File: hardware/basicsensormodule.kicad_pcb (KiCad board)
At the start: 2 copper layers, 130.2 x 52.1 mm, 76 parts, among them J102 SENSOR, J401 USART, J601 RJ45, J602 RJ45, U201 MCP2551-I/SN, U202 MCP2515-E/ST-SOIC18, U301 LM324, U401 ATMEGA328P-PU, U501 LM7805, Y201 16MHz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

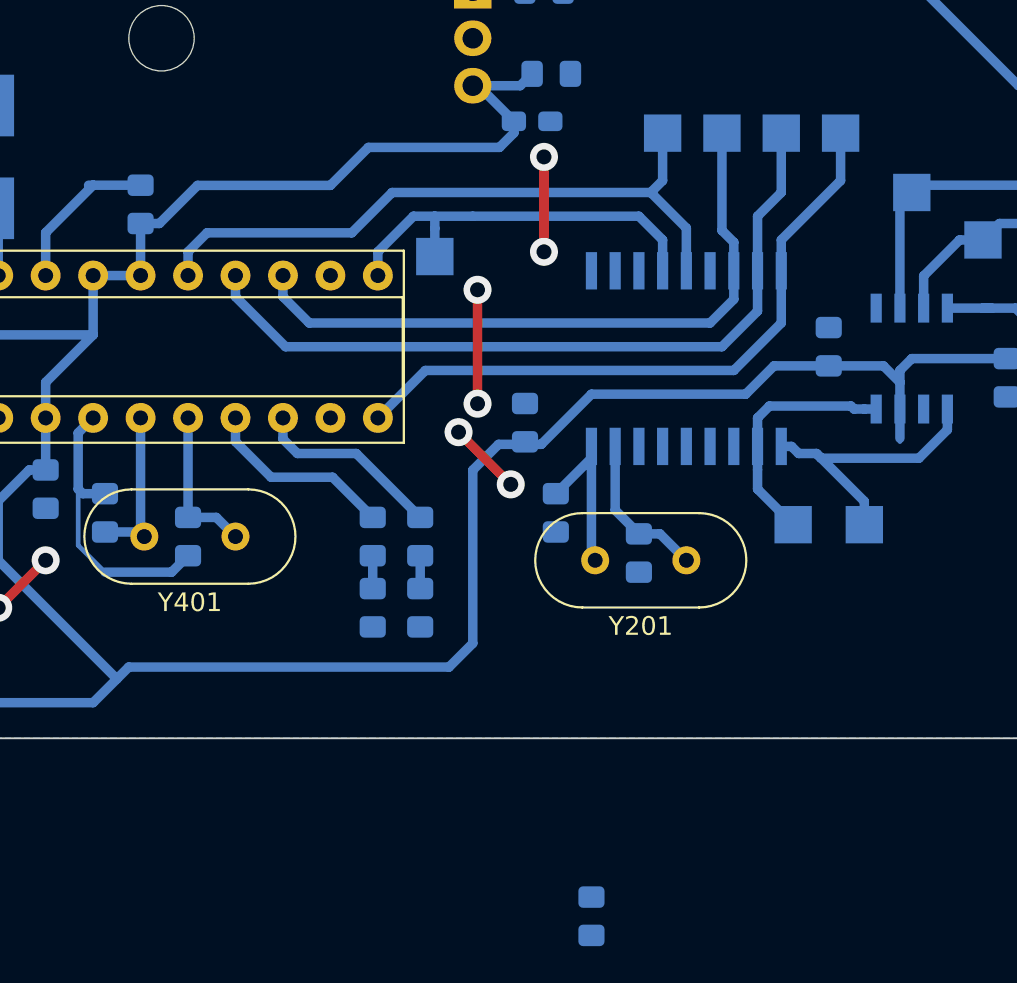
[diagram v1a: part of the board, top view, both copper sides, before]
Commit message: MCP2515 updated
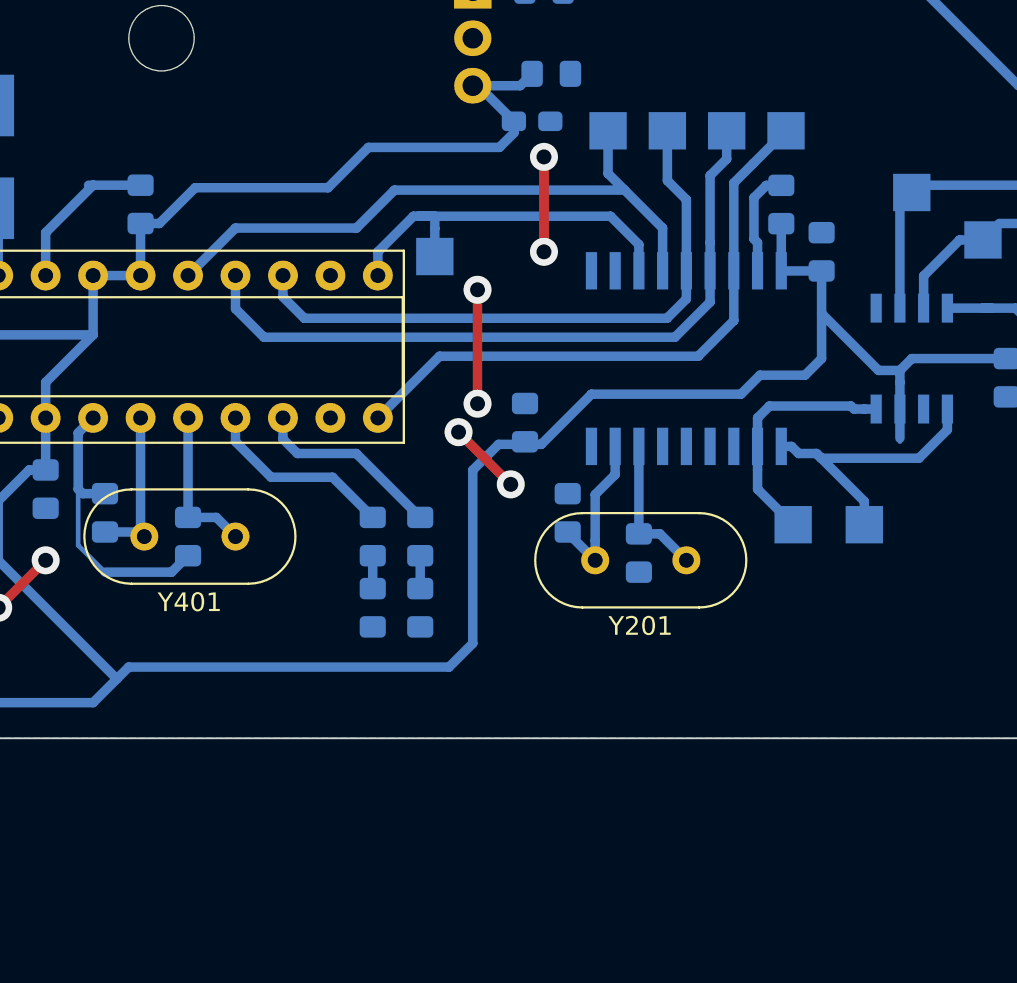
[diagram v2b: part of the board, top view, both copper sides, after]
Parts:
- U202: value MCP2515-E/ST-SOIC18 -> MCP2515-xSO
- moved R203 39.4 mm to (164.8, 96.3)
- moved C202 5.09 mm to (167.0, 98.8)
- moved TP206 2.92 mm to (155.6, 92.3)
- moved TP201 2.92 mm to (158.8, 92.3)
- moved TP202 2.92 mm to (161.9, 92.3)
- moved TP205 2.92 mm to (165.1, 92.3)
- moved C204 0.63 mm to (153.4, 112.8), turned to 90 degrees
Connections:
- U202 pad 10: GND -> Net-(U202-Pad10)
- U202 pad 12: Net-(U202-Pad12) -> /CANBUS/INT
- U202 pad 13: /CANBUS/INT -> /SCK
- U202 pad 14: /SCK -> /MOSI
- U202 pad 15: Net-(U202-Pad15) -> /MISO
- U202 pad 16: /MOSI -> /CANBUS/CS
- U202 pad 17: /MISO -> Net-(R203-Pad2)
- U202 pad 18: /CANBUS/CS -> +5V
- U202 pad 7: Net-(U202-Pad7) -> Net-(C203-Pad1)
- U202 pad 8: Net-(C203-Pad1) -> Net-(C204-Pad1)
- U202 pad 9: Net-(C204-Pad1) -> GND
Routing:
- net +5V: track 207.4 -> 217.8 mm
- net Net-(R203-Pad2): track 0.00 -> 5.72 mm
- net /MISO: track 41.0 -> 38.1 mm
- net /CANBUS/CS: track 35.2 -> 32.5 mm
- net /MOSI: track 35.5 -> 33.1 mm
- net /SCK: track 35.8 -> 34.0 mm
- net Net-(C204-Pad1): track 9.50 -> 8.66 mm
- net /CANBUS/INT: track 21.6 -> 21.1 mm
- net Net-(C203-Pad1): track 8.33 -> 7.81 mm

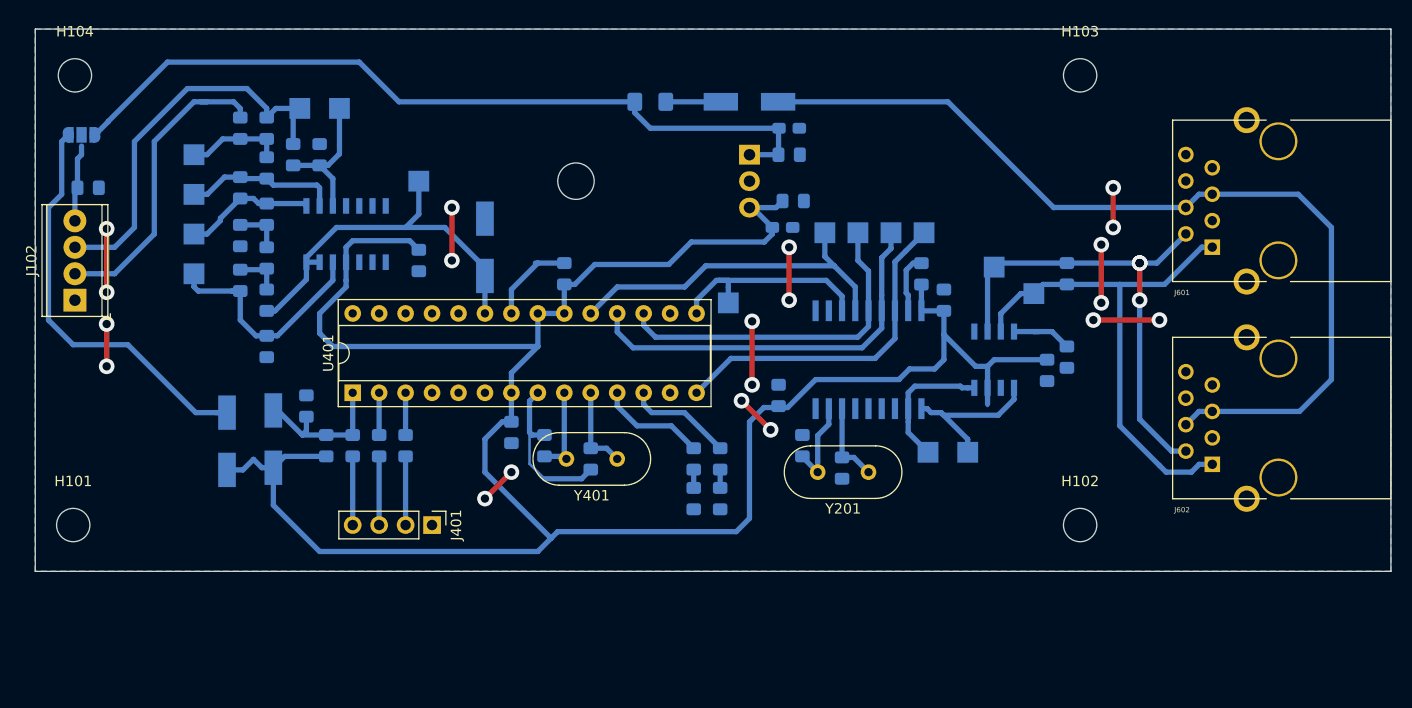
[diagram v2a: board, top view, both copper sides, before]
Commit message: Fixed simples errors and alignment
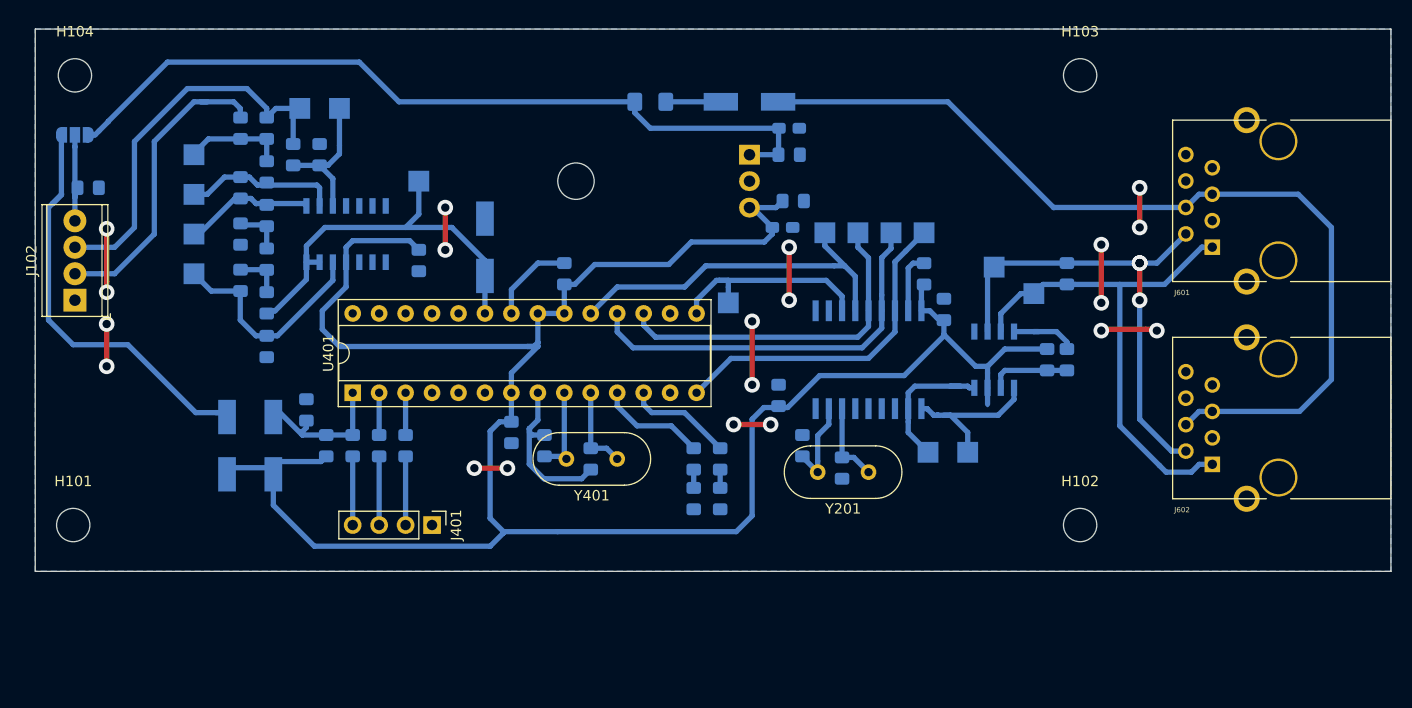
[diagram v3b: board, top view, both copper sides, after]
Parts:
- moved C205 1.03 mm to (176.9, 104.5)
- moved C202 0.89 mm to (167.0, 99.7)
- moved D401 0.63 mm to (102.6, 112.8)
- moved JP101 0.63 mm to (83.6, 82.9)
- moved D101 0.42 mm to (98.2, 112.8)
- moved R303 0.38 mm to (102.0, 86.5)
- moved C406 0.38 mm to (105.8, 109.3)
- moved C302 0.25 mm to (102.0, 99.1)
- moved R203 0.25 mm to (165.1, 96.3)
- moved R202 0.25 mm to (178.8, 104.5)
- moved C301 0.15 mm to (99.5, 92.5)
- moved R305 0.13 mm to (102.0, 90.7)
- moved R306 0.12 mm to (102.0, 94.9)
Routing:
- net GND: track 73.9 -> 81.5 mm
- net +5V: track 217.8 -> 213.1 mm
- net Net-(C102-Pad1): track 7.44 -> 9.37 mm
- net /MCU/analog1: track 37.7 -> 38.8 mm
- net /SCK: track 34.0 -> 35.0 mm
- net Net-(D101-Pad1): track 40.5 -> 41.5 mm
- net /CANBUS/RXCAN: track 13.2 -> 14.1 mm
- net Net-(C303-Pad1): track 22.1 -> 21.4 mm
- net /POWER SUPPLY/+18V_OUT: track 77.1 -> 77.8 mm

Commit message: Fixed errors Arrumado Footprint do capacitor da fonte (1u) Orientaçao dos SMDs da fonte Tirado malha em baixo de CI SMD Fotprint do 7805 foi trocada por um footprint SMD Tinha uma trilha em baixo do discipador do 7805 Tinha um jumnper em baixo do COnector O COnector dos sensores tinha footprint errado
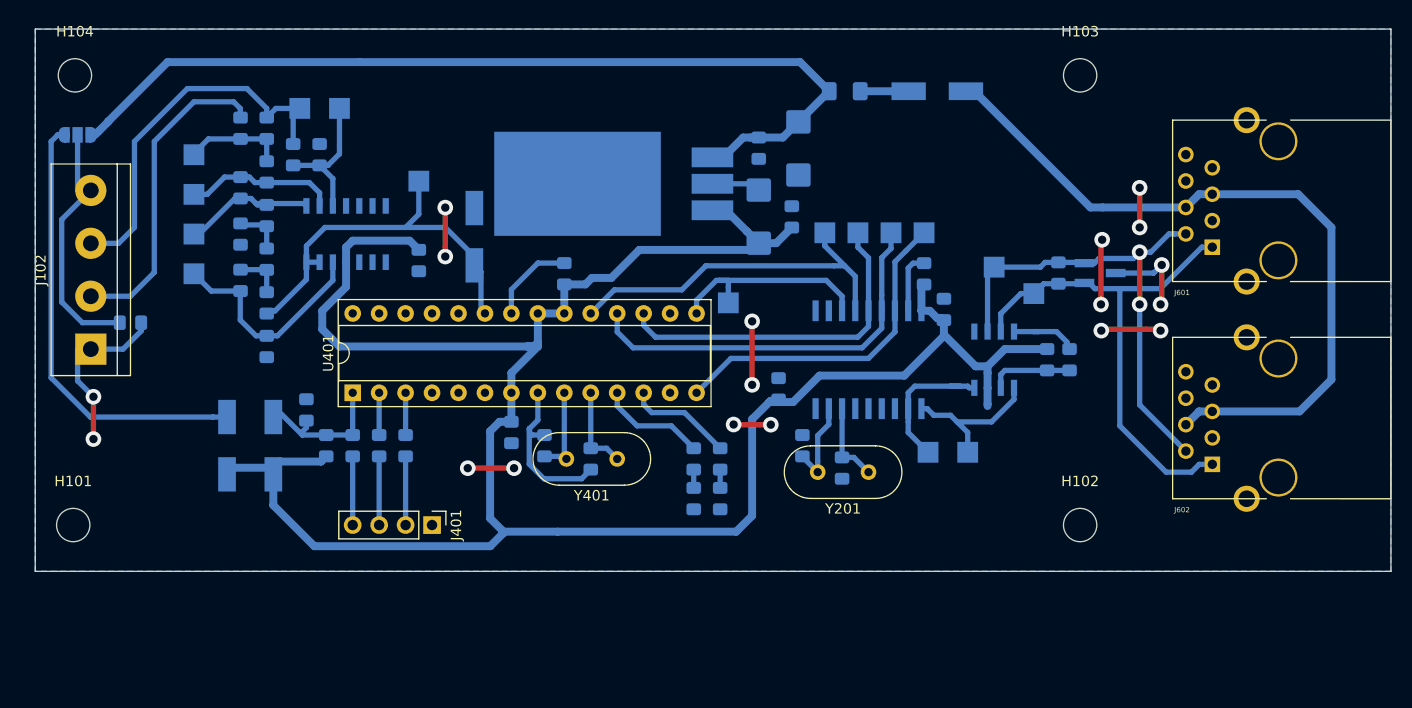
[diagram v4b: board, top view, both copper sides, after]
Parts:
- added D201: pesd1can, Package_TO_SOT_SMD:SOT-23_Handsoldering, B.Cu at (182.0, 96.2)
- C501, C504: footprint Capacitor_Tantalum_SMD:CP_EIA-2012-12_Kemet-R_Pad1.30x1.05mm_HandSolder -> Capacitor_Tantalum_SMD:CP_EIA-6032-20_AVX-F_Pad2.25x2.35mm_HandSolder
- J102: footprint TerminalBlock_Phoenix:TerminalBlock_Phoenix_MPT-0,5-4-2.54_1x04_P2.54mm_Horizontal -> TerminalBlock:TerminalBlock_bornier-4_P5.08mm
- U501: footprint Package_TO_SOT_THT:TO-220-3_Horizontal_TabDown -> KicadZeniteSolarLibrary18:TO-220-3_Horizontal_TabDown_SMD
- moved F501 18.7 mm to (157.5, 78.7)
- moved D501 18.1 mm to (166.4, 78.7)
- moved C102 13.6 mm to (88.9, 101.0)
- moved J102 4.94 mm to (85.1, 103.5)
- moved U501 4.83 mm to (143.5, 85.1)
- moved C502 2.99 mm to (149.2, 84.2), turned to 270 degrees
- moved C504 2.51 mm to (149.2, 90.8), turned to 90 degrees
- moved C501 2.13 mm to (153.0, 84.2), turned to 270 degrees
- moved C503 1.53 mm to (152.4, 90.8), turned to 90 degrees
- moved D301 1.44 mm to (121.9, 92.7)
- moved R201 0.82 mm to (178.0, 96.2)
- moved C201 0.64 mm to (151.1, 107.3)
- moved JP101 0.25 mm to (83.8, 82.9)
- moved R202 0.25 mm to (179.1, 104.5)
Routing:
- net /POWER SUPPLY/+18V_IN: track 89.6 -> 71.9 mm
- net GND: track 81.5 -> 98.1 mm, vias 20 -> 18
- net Net-(C102-Pad1): track 9.37 -> 23.2 mm
- net /POWER SUPPLY/+18V_OUT: track 77.8 -> 88.4 mm
- net +5V: track 213.1 -> 215.0 mm
- net /OPAMP/in1+: track 39.0 -> 37.3 mm
- net /CANBUS CONN/CAN_H: track 49.3 -> 50.6 mm
- net /CANBUS/TXCAN: track 16.0 -> 14.8 mm
- net Net-(D101-Pad1): track 41.5 -> 42.7 mm
- net Net-(R301-Pad1): track 12.5 -> 13.6 mm
- net /OPAMP/in1-: track 29.7 -> 30.6 mm
- net Net-(D501-Pad1): track 5.29 -> 4.65 mm
- net /CANBUS CONN/CAN_L: track 46.9 -> 47.4 mm, vias 3 -> 2

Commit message: Pads augmented to a better solder reinforcement, panel created and plotted.
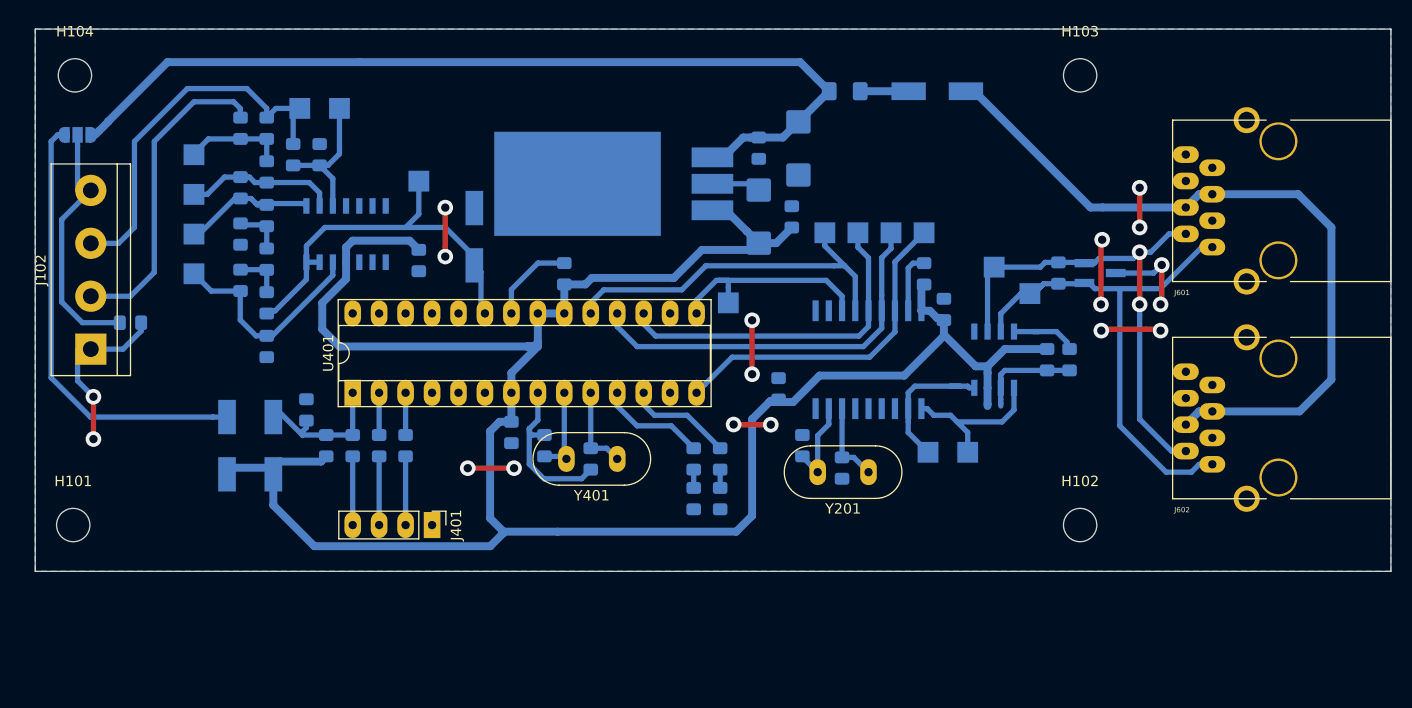
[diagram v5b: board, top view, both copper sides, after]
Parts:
- moved TP207 0.38 mm to (175.3, 98.2)
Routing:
- net GND: track 98.1 -> 99.9 mm
- net /CANBUS CONN/CAN_L: track 47.4 -> 48.2 mm
- net /CANBUS/TXCAN: track 14.8 -> 15.4 mm
- net /SCK: track 35.0 -> 35.6 mm
